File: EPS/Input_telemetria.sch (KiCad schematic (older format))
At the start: 18 parts

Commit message: Updated schematics
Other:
- note added: "140k"
- note added: "180k"
- note added: "Power loss at 500mA\nR P %(2,2W) \n0.02 5mW 0 \n0.05 12,5mW 0,5 \n0.1 25mW 1,1 \n0.2 50mW 2,3 \n0.5 125mW 5,7%"
- note added: "Resistor values for voltage dividers:\n5.5V max :\n180k/(140k + 180k)*5.5V = 3.1V"
- note removed: "Resistor values for voltage dividers:\nTODO"
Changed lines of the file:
@@
 LIBS:max40200
 LIBS:tps7a7002
+LIBS:max5395
 LIBS:EPS-cache
 EELAYER 25 0
@@
 	6600 1500 6425 1500
 Wire Wire Line
-	6600 950  6600 1500
+	6600 950  6600 1300
+Wire Wire Line
+	6600 1300 6600 1500
 Connection ~ 6600 1300
 $Comp
@@
 	5425 1800 5425 2300
 Wire Wire Line
-	5275 2300 5825 2300
-Wire Wire Line
-	6125 2300 6700 2300
+	5275 2300 5425 2300
+Wire Wire Line
+	5425 2300 5825 2300
+Wire Wire Line
+	6125 2300 6525 2300
+Wire Wire Line
+	6525 2300 6700 2300
 Wire Wire Line
 	6525 2300 6525 1800
@@
 	4650 1975 4650 1875
 Wire Wire Line
-	4525 1500 5500 1500
+	4525 1500 4650 1500
+Wire Wire Line
+	4650 1500 5500 1500
 Wire Wire Line
 	4650 1500 4650 1575
@@
 	6525 3225 6350 3225
 Wire Wire Line
-	6525 2675 6525 3225
+	6525 2675 6525 3025
+Wire Wire Line
+	6525 3025 6525 3225
 Connection ~ 6525 3025
 $Comp
@@
 	5350 3525 5350 4025
 Wire Wire Line
-	5200 4025 5750 4025
-Wire Wire Line
-	6050 4025 6625 4025
+	5200 4025 5350 4025
+Wire Wire Line
+	5350 4025 5750 4025
+Wire Wire Line
+	6050 4025 6450 4025
+Wire Wire Line
+	6450 4025 6625 4025
 Wire Wire Line
 	6450 4025 6450 3525
@@
 	4575 3700 4575 3600
 Wire Wire Line
-	4450 3225 5425 3225
+	4450 3225 4575 3225
+Wire Wire Line
+	4575 3225 5425 3225
 Wire Wire Line
 	4575 3225 4575 3300
@@
 	6450 4900 6275 4900
 Wire Wire Line
-	6450 4350 6450 4900
+	6450 4350 6450 4700
+Wire Wire Line
+	6450 4700 6450 4900
 Connection ~ 6450 4700
 $Comp
@@
 	5275 5200 5275 5700
 Wire Wire Line
-	5125 5700 5675 5700
-Wire Wire Line
-	5975 5700 6550 5700
+	5125 5700 5275 5700
+Wire Wire Line
+	5275 5700 5675 5700
+Wire Wire Line
+	5975 5700 6375 5700
+Wire Wire Line
+	6375 5700 6550 5700
 Wire Wire Line
 	6375 5700 6375 5200
@@
 	4500 5375 4500 5275
 Wire Wire Line
-	4375 4900 5350 4900
+	4375 4900 4500 4900
+Wire Wire Line
+	4500 4900 5350 4900
 Wire Wire Line
 	4500 4900 4500 4975
@@
 	8250 1150 8250 1425
 Wire Wire Line
-	8250 1900 8250 1725
+	8250 1900 8250 1825
+Wire Wire Line
+	8250 1825 8250 1725
 Text HLabel 8425 1825 2    60   Output ~ 0
 V1_IN
@@
 	8250 2900 8250 3175
 Wire Wire Line
-	8250 3650 8250 3475
+	8250 3650 8250 3575
+Wire Wire Line
+	8250 3575 8250 3475
 Text HLabel 8425 3575 2    60   Output ~ 0
 V2_IN
@@
 	8250 4775 8250 5050
 Wire Wire Line
-	8250 5525 8250 5350
+	8250 5525 8250 5450
+Wire Wire Line
+	8250 5450 8250 5350
 Text HLabel 8425 5450 2    60   Output ~ 0
 V3_IN
@@
 Connection ~ 8250 5450
 Text Notes 8700 1250 0    60   ~ 0
-Resistor values for voltage dividers:\nTODO
+Resistor values for voltage dividers:\n5.5V max :\n180k/(140k + 180k)*5.5V =  3.1V
+Text Notes 8425 1625 0    79   ~ 0
+180k
+Text Notes 8425 2100 0    79   ~ 0
+140k
+Text Notes 1050 4300 0    79   ~ 0
+Power loss at 500mA\nR					P						%(2,2W)		\n0.02		5mW						0			\n0.05		12,5mW		0,5			\n0.1			25mW				1,1			\n0.2			50mW				2,3			\n0.5			125mW			5,7%
 $EndSCHEMATC

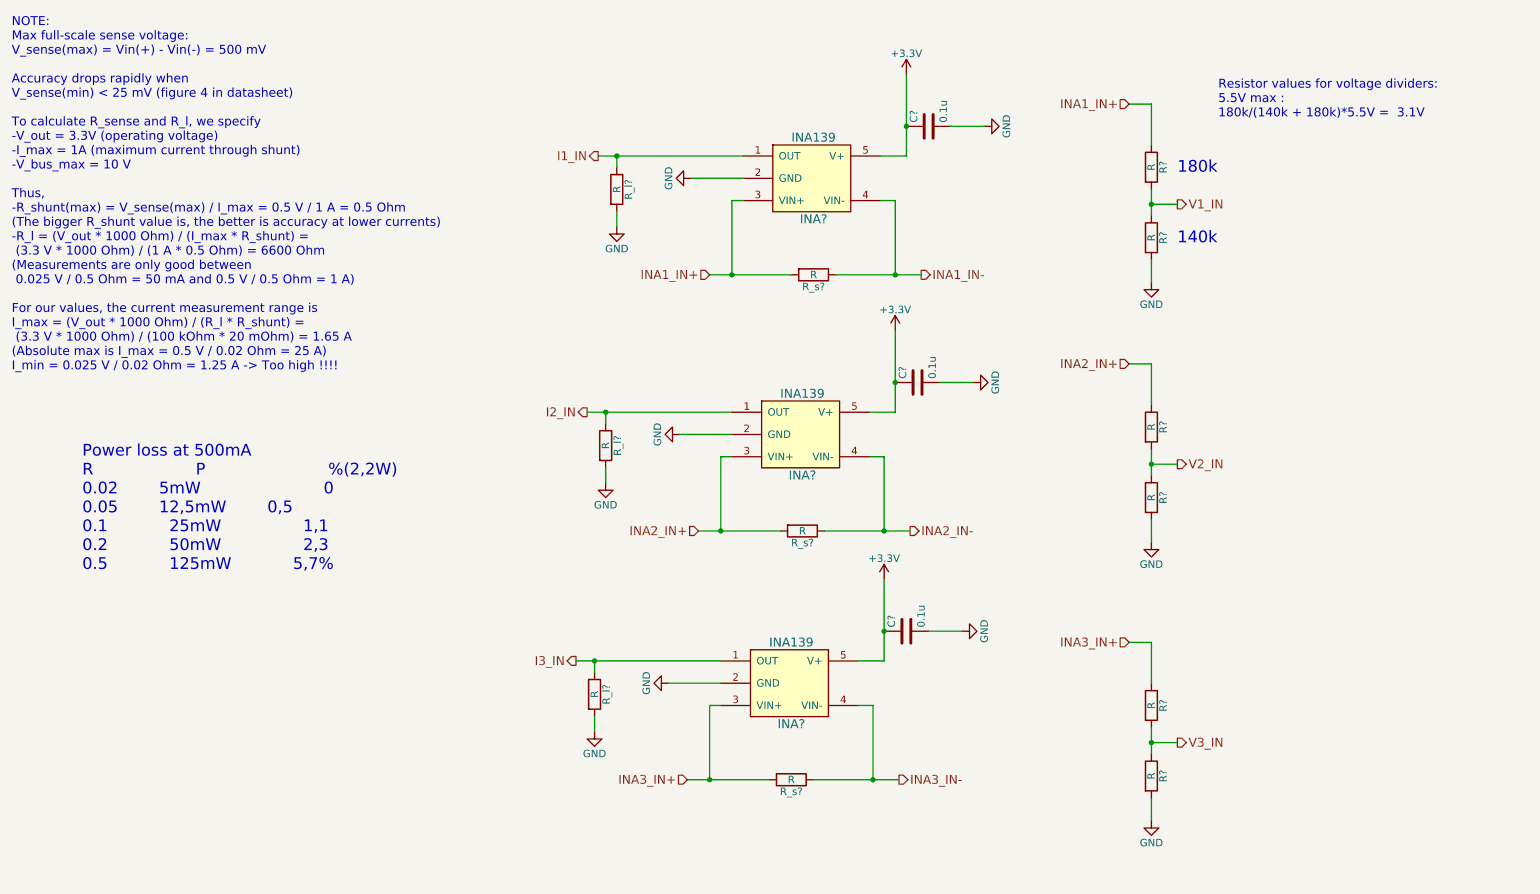
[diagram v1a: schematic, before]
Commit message: Updated Schematics
Added:
- digital pot
- digital loads
- updated  switch sheet to block two ways before battery
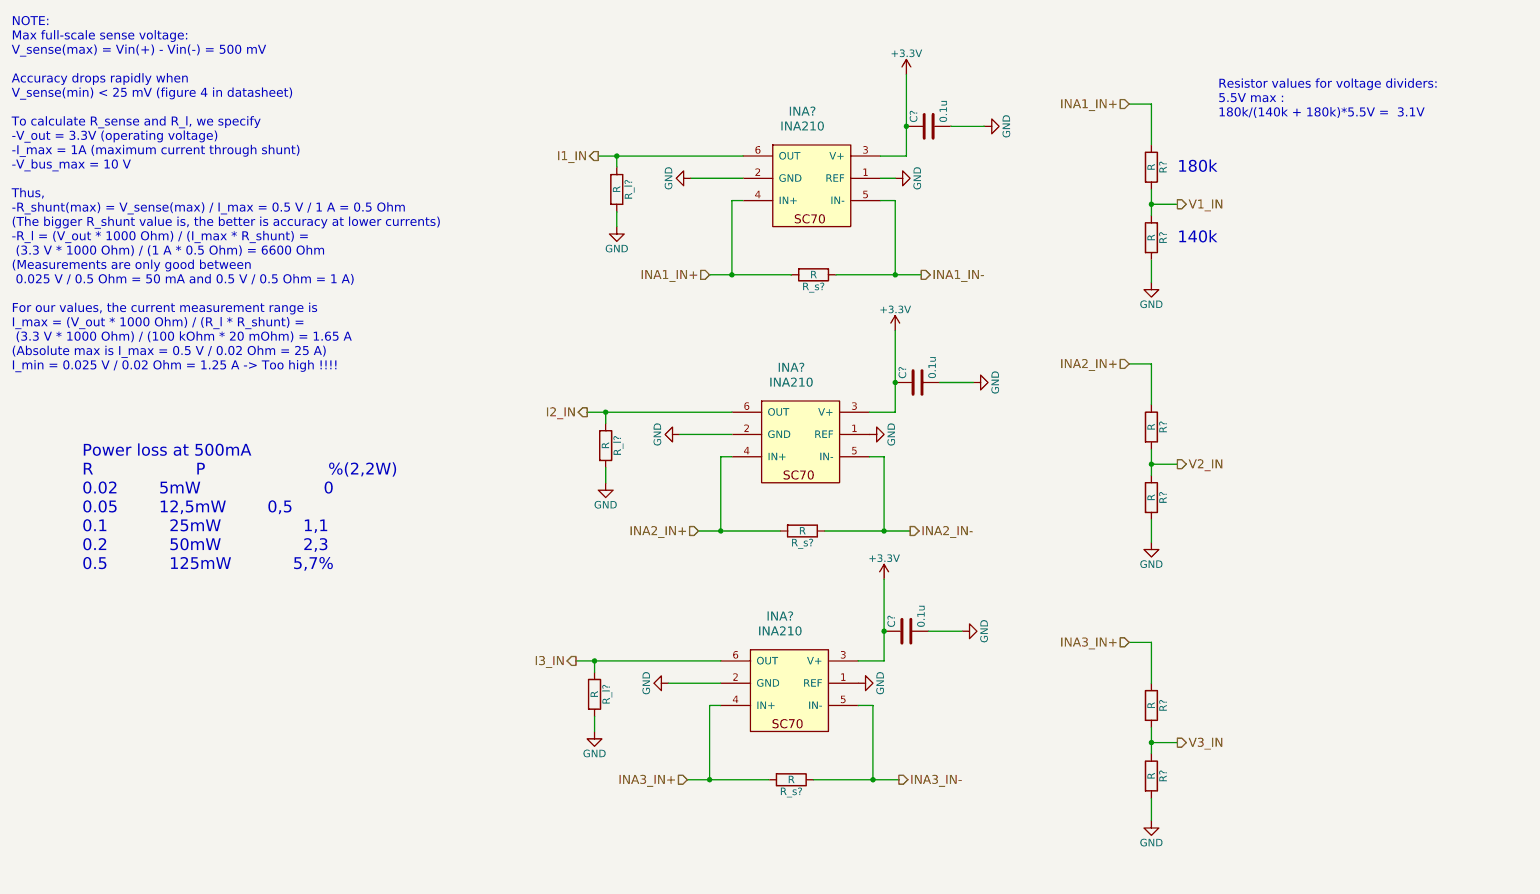
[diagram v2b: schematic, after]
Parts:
- removed INA? (x3): INA139, symbol INA139
- added INA? (x3): INA210, symbol INA210
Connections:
- net +3V3: now also INA?.3 (V+), INA?.3 (V+), INA?.3 (V+)
- net GND: now also INA?.1 (REF), INA?.1 (REF), INA?.1 (REF), INA?.2 (GND), INA?.2 (GND), INA?.2 (GND)
- net I1_IN: now also INA?.6 (OUT)
- net I2_IN: now also INA?.6 (OUT)
- net I3_IN: now also INA?.6 (OUT)
- net INA1_IN+: now also INA?.4 (IN+)
- net INA1_IN-: now also INA?.5 (IN-)
- net INA2_IN+: now also INA?.4 (IN+)
- net INA2_IN-: now also INA?.5 (IN-)
- net INA3_IN+: now also INA?.4 (IN+)
- net INA3_IN-: now also INA?.5 (IN-)
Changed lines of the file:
@@
 LIBS:tps7a7002
 LIBS:max5395
+LIBS:ina210
+LIBS:ncs20071
 LIBS:EPS-cache
 EELAYER 25 0
@@
 $Descr A4 11693 8268
 encoding utf-8
-Sheet 5 13
+Sheet 5 14
 Title "Input telemetria"
 Date "2018-02-11"
@@
 $EndDescr
 $Comp
-L INA139 INA?
-U 1 1 5A814367
-P 5975 1650
-F 0 "INA?" H 5975 1375 60  0000 C CNN
-F 1 "INA139" H 5975 1925 60  0000 C CNN
-F 2 "" H 5850 1700 60  0001 C CNN
-F 3 "" H 5850 1700 60  0001 C CNN
-	1    5975 1650
-	1    0    0    -1
-$EndComp
-$Comp
 L R R_s?
 U 1 1 5A8145F3
@@
 	6600 1500 6425 1500
 Wire Wire Line
-	6600 950  6600 1300
-Wire Wire Line
-	6600 1300 6600 1500
+	6600 950  6600 1500
 Connection ~ 6600 1300
 $Comp
@@
 	5425 1800 5425 2300
 Wire Wire Line
-	5275 2300 5425 2300
-Wire Wire Line
-	5425 2300 5825 2300
-Wire Wire Line
-	6125 2300 6525 2300
-Wire Wire Line
-	6525 2300 6700 2300
+	5275 2300 5825 2300
+Wire Wire Line
+	6125 2300 6700 2300
 Wire Wire Line
 	6525 2300 6525 1800
@@
 	4650 1975 4650 1875
 Wire Wire Line
-	4525 1500 4650 1500
-Wire Wire Line
-	4650 1500 5500 1500
+	4525 1500 5500 1500
 Wire Wire Line
 	4650 1500 4650 1575
@@
 Connection ~ 6525 2300
 $Comp
-L INA139 INA?
-U 1 1 5A818439
-P 5900 3375
-F 0 "INA?" H 5900 3100 60  0000 C CNN
-F 1 "INA139" H 5900 3650 60  0000 C CNN
-F 2 "" H 5775 3425 60  0001 C CNN
-F 3 "" H 5775 3425 60  0001 C CNN
-	1    5900 3375
-	1    0    0    -1
-$EndComp
-$Comp
 L R R_s?
 U 1 1 5A81843F
@@
 	6525 3225 6350 3225
 Wire Wire Line
-	6525 2675 6525 3025
-Wire Wire Line
-	6525 3025 6525 3225
+	6525 2675 6525 3225
 Connection ~ 6525 3025
 $Comp
@@
 	5350 3525 5350 4025
 Wire Wire Line
-	5200 4025 5350 4025
-Wire Wire Line
-	5350 4025 5750 4025
-Wire Wire Line
-	6050 4025 6450 4025
-Wire Wire Line
-	6450 4025 6625 4025
+	5200 4025 5750 4025
+Wire Wire Line
+	6050 4025 6625 4025
 Wire Wire Line
 	6450 4025 6450 3525
@@
 	4575 3700 4575 3600
 Wire Wire Line
-	4450 3225 4575 3225
-Wire Wire Line
-	4575 3225 5425 3225
+	4450 3225 5425 3225
 Wire Wire Line
 	4575 3225 4575 3300
@@
 Connection ~ 6450 4025
 $Comp
-L INA139 INA?
-U 1 1 5A818579
-P 5825 5050
-F 0 "INA?" H 5825 4775 60  0000 C CNN
-F 1 "INA139" H 5825 5325 60  0000 C CNN
-F 2 "" H 5700 5100 60  0001 C CNN
-F 3 "" H 5700 5100 60  0001 C CNN
-	1    5825 5050
-	1    0    0    -1
-$EndComp
-$Comp
 L R R_s?
 U 1 1 5A81857F
@@
 	6450 4900 6275 4900
 Wire Wire Line
-	6450 4350 6450 4700
-Wire Wire Line
-	6450 4700 6450 4900
+	6450 4350 6450 4900
 Connection ~ 6450 4700
 $Comp
@@
 	5275 5200 5275 5700
 Wire Wire Line
-	5125 5700 5275 5700
-Wire Wire Line
-	5275 5700 5675 5700
-Wire Wire Line
-	5975 5700 6375 5700
-Wire Wire Line
-	6375 5700 6550 5700
+	5125 5700 5675 5700
+Wire Wire Line
+	5975 5700 6550 5700
 Wire Wire Line
 	6375 5700 6375 5200
@@
 	4500 5375 4500 5275
 Wire Wire Line
-	4375 4900 4500 4900
-Wire Wire Line
-	4500 4900 5350 4900
+	4375 4900 5350 4900
 Wire Wire Line
 	4500 4900 4500 4975
@@
 	8250 1150 8250 1425
 Wire Wire Line
-	8250 1900 8250 1825
-Wire Wire Line
-	8250 1825 8250 1725
+	8250 1725 8250 1900
 Text HLabel 8425 1825 2    60   Output ~ 0
 V1_IN
@@
 	8250 2900 8250 3175
 Wire Wire Line
-	8250 3650 8250 3575
-Wire Wire Line
-	8250 3575 8250 3475
+	8250 3475 8250 3650
 Text HLabel 8425 3575 2    60   Output ~ 0
 V2_IN
@@
 	8250 4775 8250 5050
 Wire Wire Line
-	8250 5525 8250 5450
-Wire Wire Line
-	8250 5450 8250 5350
+	8250 5350 8250 5525
 Text HLabel 8425 5450 2    60   Output ~ 0
 V3_IN
@@
 Text Notes 1050 4300 0    79   ~ 0
 Power loss at 500mA\nR					P						%(2,2W)		\n0.02		5mW						0			\n0.05		12,5mW		0,5			\n0.1			25mW				1,1			\n0.2			50mW				2,3			\n0.5			125mW			5,7%
+$Comp
+L INA210 INA?
+U 1 1 5A8C5757
+P 5700 1425
+F 0 "INA?" H 5900 1650 60  0000 C CNN
+F 1 "INA210" H 5900 1550 60  0000 C CNN
+F 2 "" H 5900 1550 60  0001 C CNN
+F 3 "" H 5900 1550 60  0001 C CNN
+	1    5700 1425
+	1    0    0    -1
+$EndComp
+$Comp
+L GND #PWR?
+U 1 1 5A8C57FE
+P 6525 1650
+F 0 "#PWR?" H 6525 1400 50  0001 C CNN
+F 1 "GND" H 6525 1500 50  0000 C CNN
+F 2 "" H 6525 1650 50  0001 C CNN
+F 3 "" H 6525 1650 50  0001 C CNN
+	1    6525 1650
+	0    -1   -1   0
+$EndComp
+Wire Wire Line
+	6425 1650 6525 1650
+$Comp
+L INA210 INA?
+U 1 1 5A8C5BC2
+P 5625 3150
+F 0 "INA?" H 5825 3375 60  0000 C CNN
+F 1 "INA210" H 5825 3275 60  0000 C CNN
+F 2 "" H 5825 3275 60  0001 C CNN
+F 3 "" H 5825 3275 60  0001 C CNN
+	1    5625 3150
+	1    0    0    -1
+$EndComp
+$Comp
+L INA210 INA?
+U 1 1 5A8C5CFE
+P 5550 4825
+F 0 "INA?" H 5750 5050 60  0000 C CNN
+F 1 "INA210" H 5750 4950 60  0000 C CNN
+F 2 "" H 5750 4950 60  0001 C CNN
+F 3 "" H 5750 4950 60  0001 C CNN
+	1    5550 4825
+	1    0    0    -1
+$EndComp
+$Comp
+L GND #PWR?
+U 1 1 5A8C5D86
+P 6350 3375
+F 0 "#PWR?" H 6350 3125 50  0001 C CNN
+F 1 "GND" H 6350 3225 50  0000 C CNN
+F 2 "" H 6350 3375 50  0001 C CNN
+F 3 "" H 6350 3375 50  0001 C CNN
+	1    6350 3375
+	0    -1   -1   0
+$EndComp
+$Comp
+L GND #PWR?
+U 1 1 5A8C5E21
+P 6275 5050
+F 0 "#PWR?" H 6275 4800 50  0001 C CNN
+F 1 "GND" H 6275 4900 50  0000 C CNN
+F 2 "" H 6275 5050 50  0001 C CNN
+F 3 "" H 6275 5050 50  0001 C CNN
+	1    6275 5050
+	0    -1   -1   0
+$EndComp
 $EndSCHEMATC

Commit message: Finalized SCH (beta version) and started pcb
Capacitor banks might need to be reassigned to other locations.
No RBF pin on this SCH or PCB.
Battery gound deployment switch is fully mechanical (no mosfet switch on low side).
PCB of the prototype started. Main power converters and current measuring devices layed out.
SCH still requires ESD protection diodes!
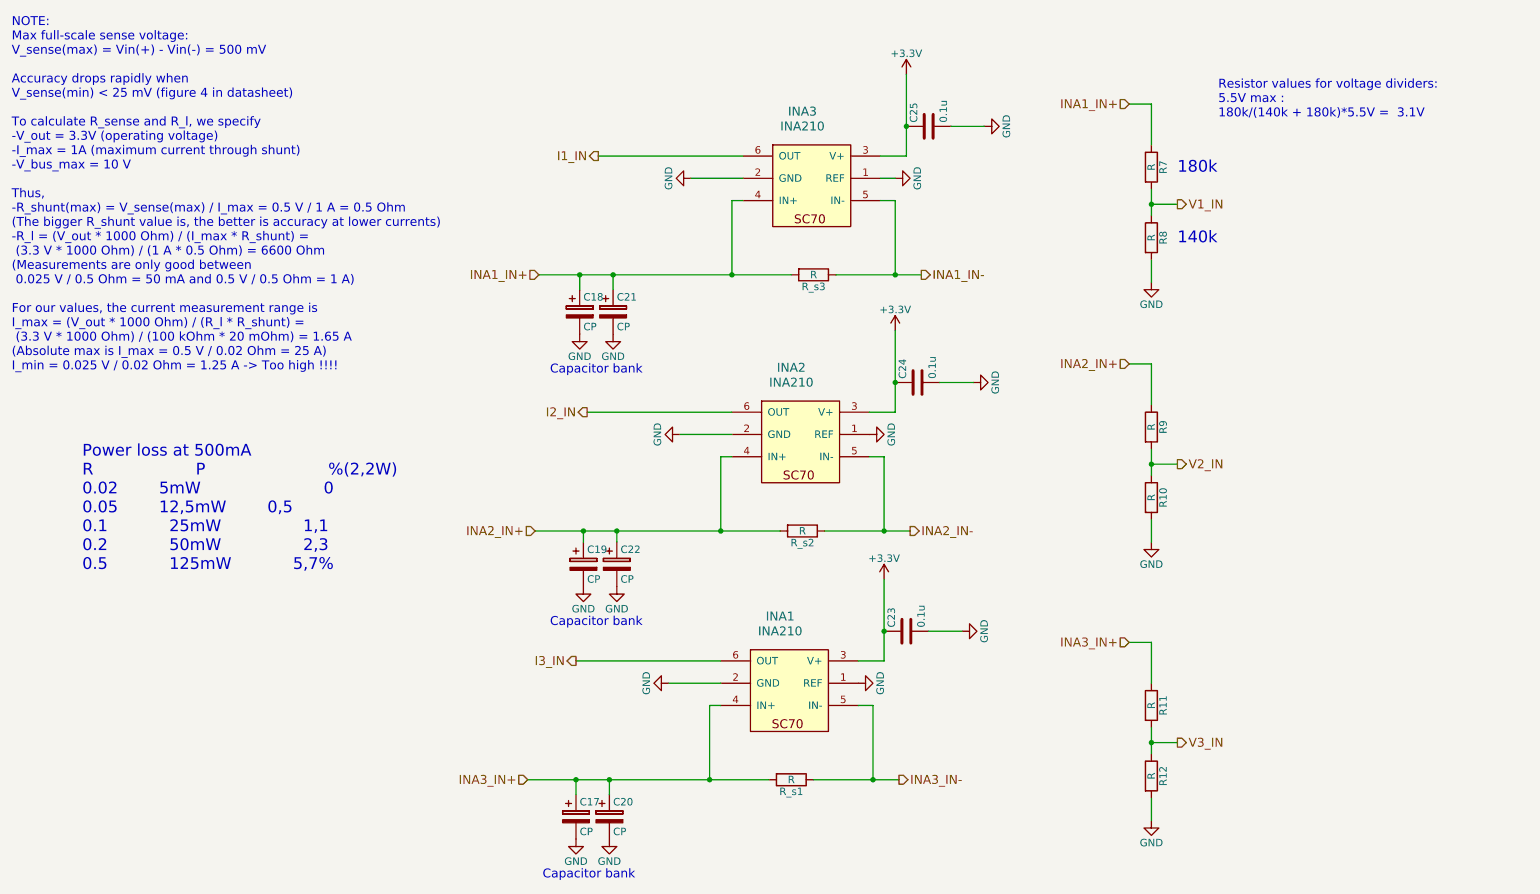
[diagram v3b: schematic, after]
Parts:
- removed R_l? (x3): R, symbol R
- added C17, C18, C19, C20, C21, C22: CP, Capacitors_Tantalum_SMD:CP_Tantalum_Case-C_EIA-6032-28_Reflow, symbol CP
- C23, C24, C25: renamed from C?; footprint (none) -> Capacitors_SMD:C_0603
- INA1, INA2, INA3: renamed from INA?; footprint (none) -> TO_SOT_Packages_SMD:SOT-363_SC-70-6
- R10, R11, R12, R7, R8, R9: renamed from R?; footprint (none) -> Resistors_SMD:R_0603
- R_s1, R_s2, R_s3: renamed from R_s?; footprint (none) -> Resistors_SMD:R_0805
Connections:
- net GND: now also C17.2, C18.2, C19.2, C20.2, C21.2, C22.2
- net INA1_IN+: now also C18.1, C21.1
- net INA2_IN+: now also C19.1, C22.1
- net INA3_IN+: now also C17.1, C20.1
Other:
- note added: "Capacitor bank"
